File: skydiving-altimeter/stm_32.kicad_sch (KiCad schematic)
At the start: 12 parts, among them J1 Conn_ARM_JTAG_SWD_10, U1 STM32F103C8Tx

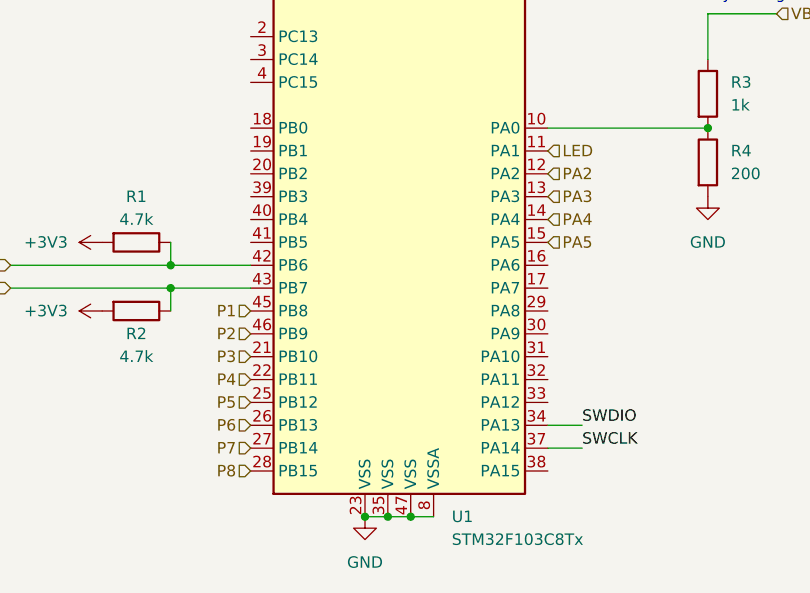
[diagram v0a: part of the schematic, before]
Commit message: Started rerouting
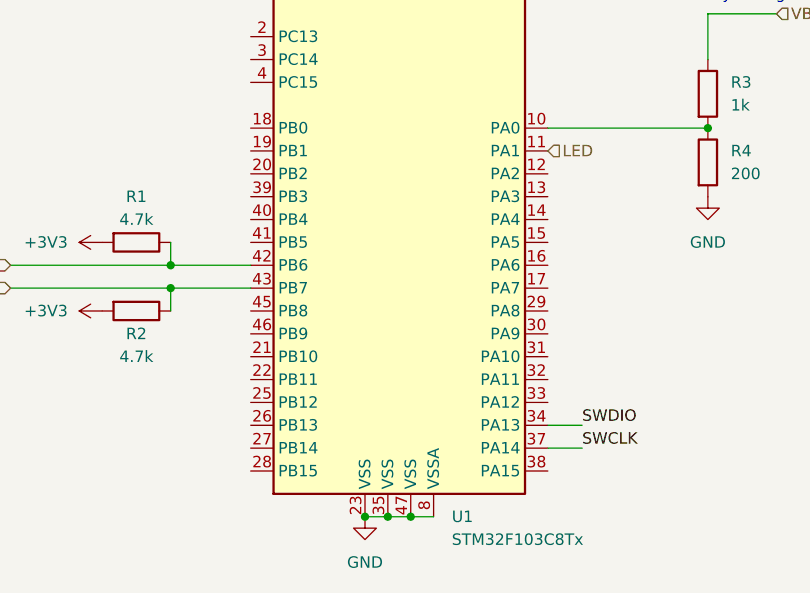
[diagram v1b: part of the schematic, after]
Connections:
- net P1: no longer names the net of U1.45 (PB8)
- net P2: no longer names the net of U1.46 (PB9)
- net P3: no longer names the net of U1.21 (PB10)
- net P4: no longer names the net of U1.22 (PB11)
- net P5: no longer names the net of U1.25 (PB12)
- net P6: no longer names the net of U1.26 (PB13)
- net P7: no longer names the net of U1.27 (PB14)
- net P8: no longer names the net of U1.28 (PB15)
- net PA2: no longer names the net of U1.12 (PA2)
- net PA3: no longer names the net of U1.13 (PA3)
- net PA4: no longer names the net of U1.14 (PA4)
- net PA5: no longer names the net of U1.15 (PA5)
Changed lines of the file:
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@@
     (effects (font (size 1.27 1.27)) (justify left bottom))
   )
-  (hierarchical_label "P6" (shape input) (at 154.94 137.16 180)
-    (effects (font (size 1.27 1.27)) (justify right))
-  )
   (hierarchical_label "SDA" (shape input) (at 128.27 121.92 180)
-    (effects (font (size 1.27 1.27)) (justify right))
-  )
-  (hierarchical_label "PA2" (shape input) (at 187.96 109.22 0)
-    (effects (font (size 1.27 1.27)) (justify left))
-  )
-  (hierarchical_label "P5" (shape input) (at 154.94 134.62 180)
-    (effects (font (size 1.27 1.27)) (justify right))
-  )
-  (hierarchical_label "P1" (shape input) (at 154.94 124.46 180)
     (effects (font (size 1.27 1.27)) (justify right))
   )
@@
     (effects (font (size 1.27 1.27)) (justify left))
   )
-  (hierarchical_label "P2" (shape input) (at 154.94 127 180)
-    (effects (font (size 1.27 1.27)) (justify right))
-  )
-  (hierarchical_label "PA5" (shape input) (at 187.96 116.84 0)
-    (effects (font (size 1.27 1.27)) (justify left))
-  )
-  (hierarchical_label "P4" (shape input) (at 154.94 132.08 180)
-    (effects (font (size 1.27 1.27)) (justify right))
-  )
-  (hierarchical_label "PA3" (shape input) (at 187.96 111.76 0)
-    (effects (font (size 1.27 1.27)) (justify left))
-  )
-  (hierarchical_label "P7" (shape input) (at 154.94 139.7 180)
-    (effects (font (size 1.27 1.27)) (justify right))
-  )
   (hierarchical_label "VBAT" (shape input) (at 213.36 91.44 0)
-    (effects (font (size 1.27 1.27)) (justify left))
-  )
-  (hierarchical_label "P3" (shape input) (at 154.94 129.54 180)
-    (effects (font (size 1.27 1.27)) (justify right))
-  )
-  (hierarchical_label "PA4" (shape input) (at 187.96 114.3 0)
     (effects (font (size 1.27 1.27)) (justify left))
   )
@@
     (effects (font (size 1.27 1.27)) (justify right))
   )
-  (hierarchical_label "P8" (shape input) (at 154.94 142.24 180)
-    (effects (font (size 1.27 1.27)) (justify right))
-  )

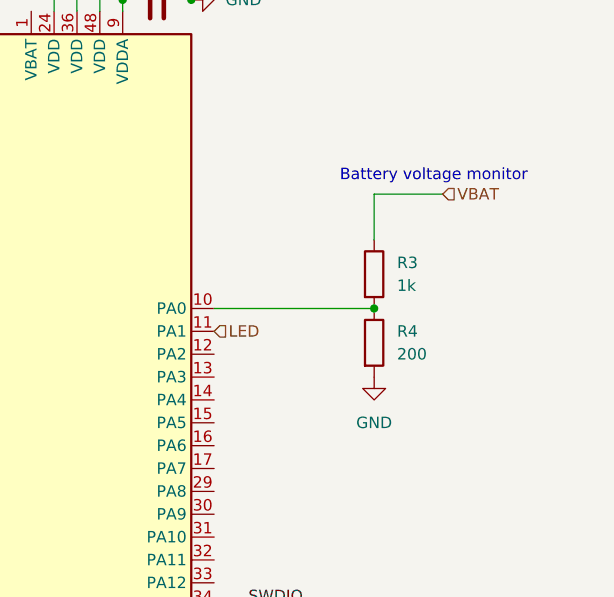
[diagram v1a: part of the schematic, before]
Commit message: Finished reroute
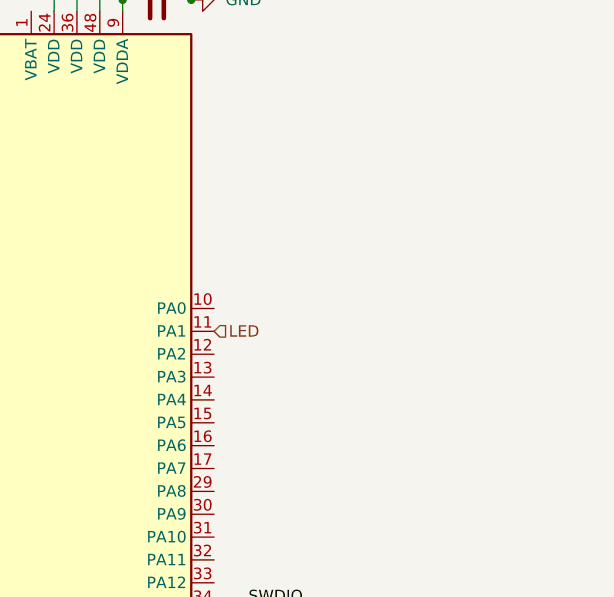
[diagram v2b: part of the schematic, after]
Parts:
- removed R3: 1k, Resistor_SMD:R_0805_2012Metric, symbol Device:R
- removed R4: 200, Resistor_SMD:R_0805_2012Metric, symbol Device:R
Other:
- note removed: "Battery voltage monitor"
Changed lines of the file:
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@@
   (junction (at 185.42 69.85) (diameter 0) (color 0 0 0 0)
   )
-  (junction (at 205.74 104.14) (diameter 0) (color 0 0 0 0)
-  )
   (junction (at 161.29 52.07) (diameter 0) (color 0 0 0 0)
   )
@@
     (stroke (width 0) (type default) (color 0 0 0 0))
   )
-  (wire (pts (xy 205.74 91.44) (xy 205.74 96.52))
-    (stroke (width 0) (type default) (color 0 0 0 0))
-  )
   (wire (pts (xy 175.26 60.96) (xy 175.26 71.12))
     (stroke (width 0) (type default) (color 0 0 0 0))
@@
     (stroke (width 0) (type default) (color 0 0 0 0))
   )
-  (wire (pts (xy 213.36 91.44) (xy 205.74 91.44))
-    (stroke (width 0) (type default) (color 0 0 0 0))
-  )
   (wire (pts (xy 167.64 147.32) (xy 170.18 147.32))
     (stroke (width 0) (type default) (color 0 0 0 0))
@@
   (wire (pts (xy 161.29 43.18) (xy 161.29 52.07))
     (stroke (width 0) (type default) (color 0 0 0 0))
-  )
-  (wire (pts (xy 187.96 104.14) (xy 205.74 104.14))
-    (stroke (width 0) (type default) (color 0 0 0 0))
-  )
-  (text "Battery voltage monitor" (at 201.93 90.17 0)
-    (effects (font (size 1.27 1.27)) (justify left bottom))
   )
   (label "SWDIO" (at 99.06 111.76 0)
@@
     (effects (font (size 1.27 1.27)) (justify left))
   )
-  (hierarchical_label "VBAT" (shape input) (at 213.36 91.44 0)
-    (effects (font (size 1.27 1.27)) (justify left))
-  )
   (hierarchical_label "SCL" (shape input) (at 128.27 119.38 180)
     (effects (font (size 1.27 1.27)) (justify right))
@@
     )
     (pin "1")
-  )
-  (symbol (lib_id "Device:R") (at 205.74 107.95 0) (unit 1)
-    (in_bom yes) (on_board yes) (fields_autoplaced)
-    (property "Reference" "R4" (id 0) (at 208.28 106.6799 0)
-      (effects (font (size 1.27 1.27)) (justify left))
-    )
-    (property "Value" "200" (id 1) (at 208.28 109.2199 0)
-      (effects (font (size 1.27 1.27)) (justify left))
-    )
-    (property "Footprint" "Resistor_SMD:R_0805_2012Metric" (id 2) (at 203.962 107.95 90)
-      (effects (font (size 1.27 1.27)) hide)
-    )
-    (property "Datasheet" "~" (id 3) (at 205.74 107.95 0)
-      (effects (font (size 1.27 1.27)) hide)
-    )
-    (pin "1")
-    (pin "2")
   )
   (symbol (lib_id "power:GND") (at 167.64 147.32 0) (unit 1)
@@
     (pin "2")
   )
-  (symbol (lib_id "Device:R") (at 205.74 100.33 0) (unit 1)
-    (in_bom yes) (on_board yes) (fields_autoplaced)
-    (property "Reference" "R3" (id 0) (at 208.28 99.0599 0)
-      (effects (font (size 1.27 1.27)) (justify left))
-    )
-    (property "Value" "1k" (id 1) (at 208.28 101.5999 0)
-      (effects (font (size 1.27 1.27)) (justify left))
-    )
-    (property "Footprint" "Resistor_SMD:R_0805_2012Metric" (id 2) (at 203.962 100.33 90)
-      (effects (font (size 1.27 1.27)) hide)
-    )
-    (property "Datasheet" "~" (id 3) (at 205.74 100.33 0)
-      (effects (font (size 1.27 1.27)) hide)
-    )
-    (pin "1")
-    (pin "2")
-  )
   (symbol (lib_id "power:+3V3") (at 146.05 58.42 90) (unit 1)
     (in_bom yes) (on_board yes) (fields_autoplaced)
@@
       (effects (font (size 1.27 1.27)) hide)
     )
-    (pin "1")
-  )
-  (symbol (lib_id "power:GND") (at 205.74 111.76 0) (unit 1)
-    (in_bom yes) (on_board yes) (fields_autoplaced)
-    (property "Reference" "#PWR0111" (id 0) (at 205.74 118.11 0)
-      (effects (font (size 1.27 1.27)) hide)
-    )
-    (property "Value" "GND" (id 1) (at 205.74 116.84 0))
-    (property "Footprint" "" (id 2) (at 205.74 111.76 0)
-      (effects (font (size 1.27 1.27)) hide)
-    )
-    (property "Datasheet" "" (id 3) (at 205.74 111.76 0)
-      (effects (font (size 1.27 1.27)) hide)
-    )

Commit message: Switched most components to 0402
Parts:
- C1, C2, C3, C4, C5, C6: footprint Capacitor_SMD:C_0805_2012Metric -> Capacitor_SMD:C_0402_1005Metric
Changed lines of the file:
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@@
       (effects (font (size 1.27 1.27)))
     )
-    (property "Footprint" "Capacitor_SMD:C_0805_2012Metric" (at 172.72 53.0352 0)
+    (property "Footprint" "Capacitor_SMD:C_0402_1005Metric" (at 172.72 53.0352 0)
       (effects (font (size 1.27 1.27)) hide)
     )
@@
       (effects (font (size 1.27 1.27)))
     )
-    (property "Footprint" "Capacitor_SMD:C_0805_2012Metric" (at 175.26 61.9252 0)
+    (property "Footprint" "Capacitor_SMD:C_0402_1005Metric" (at 175.26 61.9252 0)
       (effects (font (size 1.27 1.27)) hide)
     )
@@
       (effects (font (size 1.27 1.27)))
     )
-    (property "Footprint" "Capacitor_SMD:C_0805_2012Metric" (at 177.8 70.8152 0)
+    (property "Footprint" "Capacitor_SMD:C_0402_1005Metric" (at 177.8 70.8152 0)
       (effects (font (size 1.27 1.27)) hide)
     )
@@
       (effects (font (size 1.27 1.27)) (justify left))
     )
-    (property "Footprint" "Capacitor_SMD:C_0805_2012Metric" (at 152.0952 58.42 0)
+    (property "Footprint" "Capacitor_SMD:C_0402_1005Metric" (at 152.0952 58.42 0)
       (effects (font (size 1.27 1.27)) hide)
     )
@@
       (effects (font (size 1.27 1.27)))
     )
-    (property "Footprint" "Capacitor_SMD:C_0805_2012Metric" (at 147.32 77.1652 0)
+    (property "Footprint" "Capacitor_SMD:C_0402_1005Metric" (at 147.32 77.1652 0)
       (effects (font (size 1.27 1.27)) hide)
     )
@@
       (effects (font (size 1.27 1.27)))
     )
-    (property "Footprint" "Capacitor_SMD:C_0805_2012Metric" (at 170.18 44.1452 0)
-      (effects (font (size 1.27 1.27)) hide)
-    )
+    (property "Footprint" "Capacitor_SMD:C_0402_1005Metric" (at 170.18 44.1452 0)
+      (effects (font (size 1.27 1.27)) hide)
+    )
